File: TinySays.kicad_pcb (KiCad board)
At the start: 2 copper layers, 40 x 40 mm, 31 parts, among them IC1 ATTINY85-S, P1 CONN_02X03, P2 USB_OTG, P3 CONN_01X02, SW1 Switch_SPDT_x2, U1 MCP73831

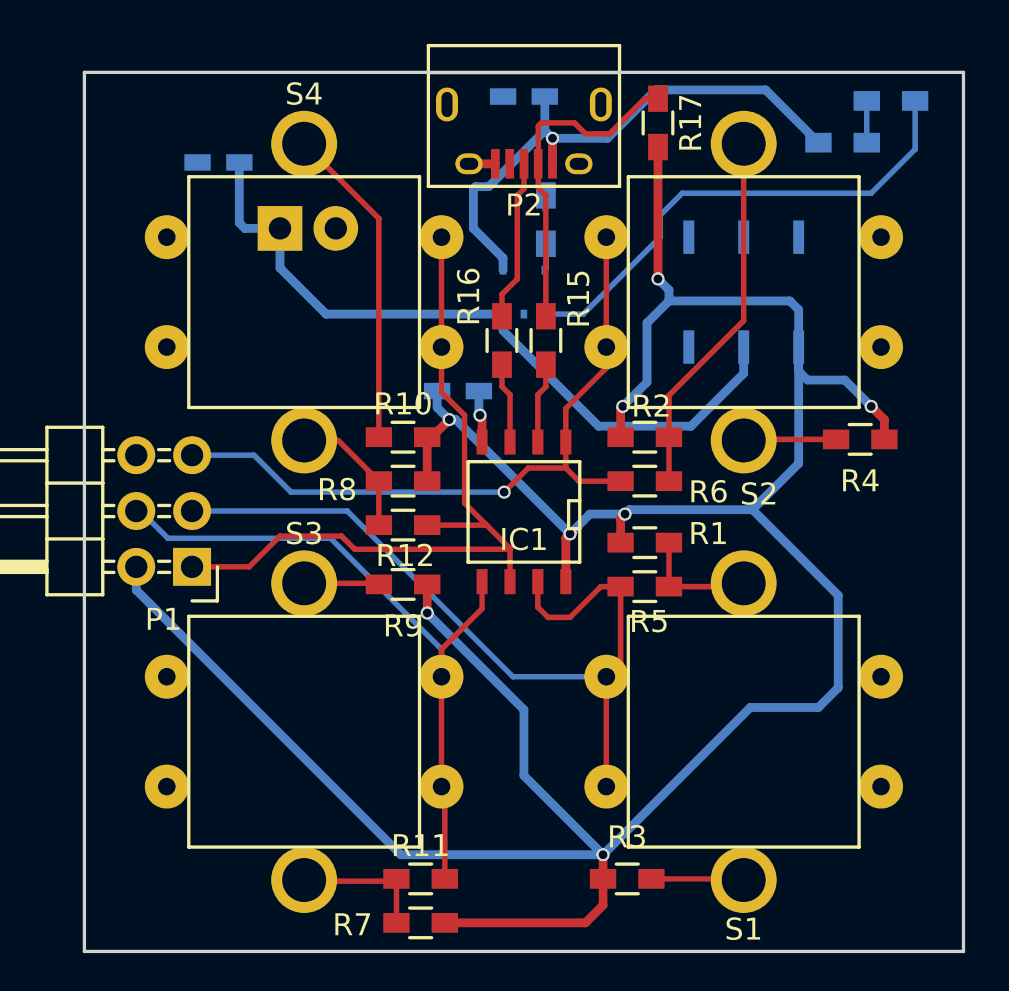
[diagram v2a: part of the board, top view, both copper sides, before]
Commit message: Cleaned up the routing a bit.
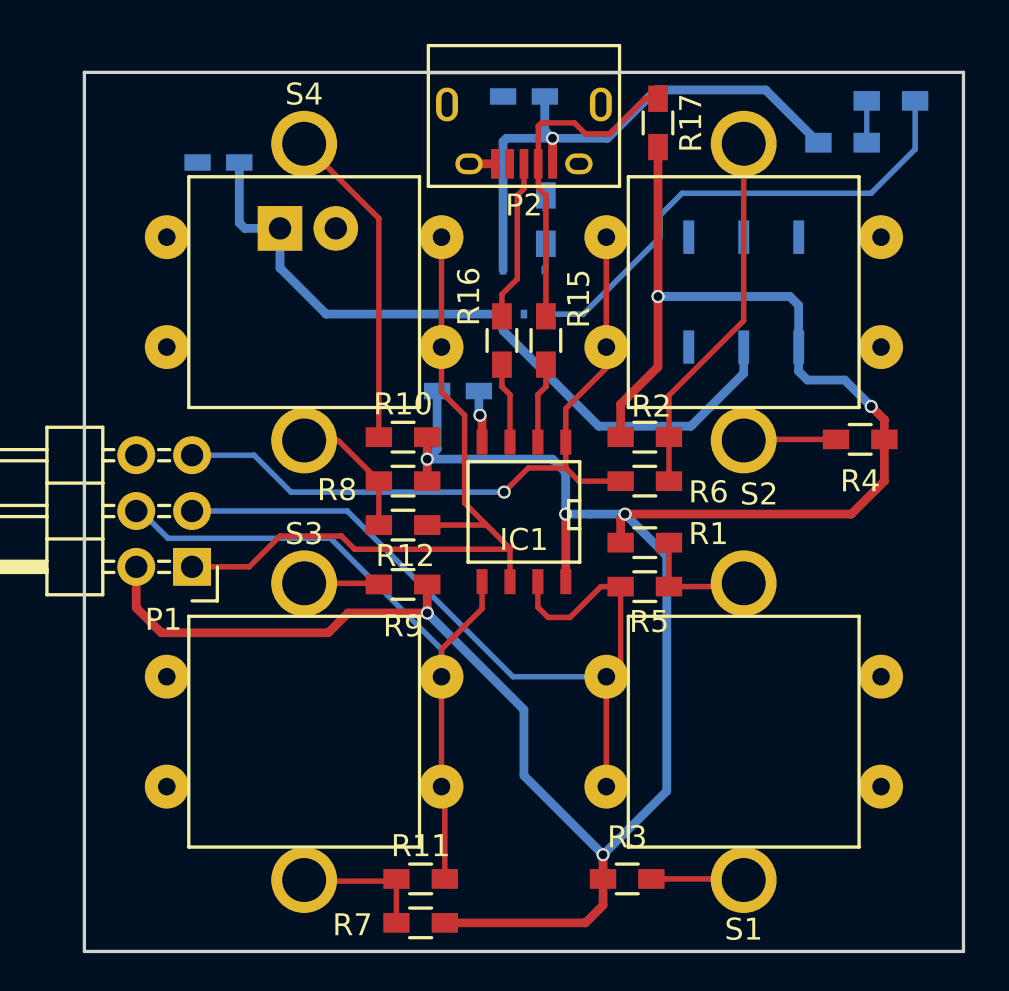
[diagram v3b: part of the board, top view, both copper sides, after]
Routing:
- net VCC: track 138.6 -> 123.8 mm, vias 8 -> 7
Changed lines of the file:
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@@
-(kicad_pcb (version 4) (host pcbnew 4.0.2-stable)
+(kicad_pcb (version 4) (host pcbnew 4.0.2-4+6225~38~ubuntu14.04.1-stable)
   (general
     (links 74)
     (no_connects 0)
-    (area 77.374999 42.175 126.000001 87.075)
+    (area 85.824999 45.424999 125.975001 85.575001)
     (thickness 1.6)
     (drawings 16)
-    (tracks 197)
+    (tracks 190)
     (zones 0)
     (modules 31)
@@
   (gr_line (start 125.9 45.5) (end 125.9 85.5) (angle 90) (layer Edge.Cuts) (width 0.15))
   (gr_line (start 85.9 45.5) (end 125.9 45.5) (angle 90) (layer Edge.Cuts) (width 0.15))
+  (segment (start 104.95 54.5) (end 104.95 48.65) (width 0.4) (layer B.Cu) (net 1))
+  (segment (start 105.1 48.5) (end 107.2 48.5) (width 0.4) (layer B.Cu) (net 1))
+  (segment (start 104.95 48.65) (end 105.1 48.5) (width 0.4) (layer B.Cu) (net 1))
   (segment (start 106.85 46.6) (end 106.85 48.15) (width 0.4) (layer B.Cu) (net 1))
-  (segment (start 106.85 48.15) (end 104.3 50.7) (width 0.4) (layer B.Cu) (net 1))
-  (segment (start 104.95 53.95) (end 104.95 54.5) (width 0.4) (layer B.Cu) (net 1))
-  (segment (start 103.6 52.6) (end 104.95 53.95) (width 0.4) (layer B.Cu) (net 1))
-  (segment (start 103.6 50.8) (end 103.6 52.6) (width 0.4) (layer B.Cu) (net 1))
-  (segment (start 103.7 50.7) (end 103.6 50.8) (width 0.4) (layer B.Cu) (net 1))
-  (segment (start 104.3 50.7) (end 103.7 50.7) (width 0.4) (layer B.Cu) (net 1))
   (segment (start 107.2 48.5) (end 109.7 48.5) (width 0.4) (layer B.Cu) (net 1))
   (segment (start 116.9 46.3) (end 119.3 48.7) (width 0.4) (layer B.Cu) (net 1))
@@
   (segment (start 103.85 61.05) (end 103.9 61.1) (width 0.4) (layer B.Cu) (net 2))
   (segment (start 104.6009 49.66254) (end 103.4009 49.66254) (width 0.4) (layer F.Cu) (net 2))
-  (segment (start 102.5 61.3) (end 102.8 61.3) (width 0.4) (layer B.Cu) (net 3))
-  (segment (start 102.8 61.3) (end 108 66.5) (width 0.4) (layer B.Cu) (net 3))
-  (segment (start 88.26 68) (end 88.26 69.06) (width 0.4) (layer B.Cu) (net 3))
-  (segment (start 100.3 81.1) (end 109.5 81.1) (width 0.4) (layer B.Cu) (net 3))
-  (segment (start 88.26 69.06) (end 100.3 81.1) (width 0.4) (layer B.Cu) (net 3))
+  (segment (start 118.4 58) (end 118.4 56.1) (width 0.4) (layer B.Cu) (net 3) (status 400000))
+  (via (at 112 55.7) (size 0.6) (drill 0.4) (layers F.Cu B.Cu) (net 3))
+  (segment (start 118 55.7) (end 112 55.7) (width 0.4) (layer B.Cu) (net 3))
+  (segment (start 118.4 56.1) (end 118 55.7) (width 0.4) (layer B.Cu) (net 3))
+  (segment (start 112 48.9) (end 112 55.7) (width 0.4) (layer F.Cu) (net 3) (status 400000))
+  (segment (start 112 55.7) (end 112 58.9) (width 0.4) (layer F.Cu) (net 3))
+  (segment (start 112 58.9) (end 110.3 60.6) (width 0.4) (layer F.Cu) (net 3))
+  (segment (start 110.3 60.6) (end 110.3 62.1) (width 0.4) (layer F.Cu) (net 3) (status 800000))
+  (segment (start 109.5 81.1) (end 112.4 78.2) (width 0.4) (layer B.Cu) (net 3))
+  (segment (start 112.4 78.2) (end 112.4 67.5) (width 0.4) (layer B.Cu) (net 3))
+  (segment (start 112.4 67.5) (end 110.5 65.6) (width 0.4) (layer B.Cu) (net 3))
+  (segment (start 110.5 65.6) (end 120.8 65.6) (width 0.4) (layer F.Cu) (net 3))
+  (segment (start 122.3 64.1) (end 122.3 62.2) (width 0.4) (layer F.Cu) (net 3))
+  (segment (start 120.8 65.6) (end 122.3 64.1) (width 0.4) (layer F.Cu) (net 3))
+  (segment (start 101.5 70.1) (end 97.9 70.1) (width 0.4) (layer F.Cu) (net 3))
+  (segment (start 88.26 69.86) (end 88.26 68) (width 0.4) (layer F.Cu) (net 3))
+  (segment (start 89.4 71) (end 88.26 69.86) (width 0.4) (layer F.Cu) (net 3))
+  (segment (start 97 71) (end 89.4 71) (width 0.4) (layer F.Cu) (net 3))
+  (segment (start 97.9 70.1) (end 97 71) (width 0.4) (layer F.Cu) (net 3))
+  (segment (start 107.8 65.6) (end 107.8 63.7) (width 0.4) (layer B.Cu) (net 3))
+  (segment (start 107.2 63.1) (end 101.5 63.1) (width 0.4) (layer B.Cu) (net 3))
+  (segment (start 107.8 63.7) (end 107.2 63.1) (width 0.4) (layer B.Cu) (net 3))
+  (via (at 101.5 63.1) (size 0.6) (drill 0.4) (layers F.Cu B.Cu) (net 3))
+  (segment (start 101.95 60) (end 101.95 62.65) (width 0.4) (layer B.Cu) (net 3))
+  (segment (start 101.95 62.65) (end 101.5 63.1) (width 0.4) (layer B.Cu) (net 3))
+  (segment (start 107.805 68.675) (end 107.805 65.605) (width 0.4) (layer F.Cu) (net 3))
+  (via (at 107.8 65.6) (size 0.6) (drill 0.4) (layers F.Cu B.Cu) (net 3))
+  (segment (start 107.805 65.605) (end 107.8 65.6) (width 0.4) (layer F.Cu) (net 3))
   (segment (start 109.5 81.1) (end 105.9 77.5) (width 0.4) (layer B.Cu) (net 3))
-  (segment (start 119.3 74.4) (end 120.2 73.5) (width 0.4) (layer B.Cu) (net 3))
-  (segment (start 116.2 74.4) (end 119.3 74.4) (width 0.4) (layer B.Cu) (net 3))
-  (segment (start 109.5 81.1) (end 116.2 74.4) (width 0.4) (layer B.Cu) (net 3))
   (segment (start 101.5 64.1) (end 101.8 64.1) (width 0.4) (layer F.Cu) (net 3))
   (segment (start 101.5 62.1) (end 101.7 62.1) (width 0.4) (layer F.Cu) (net 3))
-  (segment (start 101.7 62.1) (end 102.5 61.3) (width 0.4) (layer F.Cu) (net 3))
-  (segment (start 101.95 60.75) (end 101.95 60.1) (width 0.4) (layer B.Cu) (net 3))
-  (segment (start 102.5 61.3) (end 101.95 60.75) (width 0.4) (layer B.Cu) (net 3))
-  (via (at 102.5 61.3) (size 0.6) (drill 0.4) (layers F.Cu B.Cu) (net 3))
-  (segment (start 101.5 62.1) (end 101.5 64.1) (width 0.4) (layer F.Cu) (net 3))
+  (segment (start 101.5 62.1) (end 101.5 63.1) (width 0.4) (layer F.Cu) (net 3))
+  (segment (start 101.5 63.1) (end 101.5 64.1) (width 0.4) (layer F.Cu) (net 3))
   (segment (start 101.5 70.1) (end 101.5 68.8) (width 0.4) (layer F.Cu) (net 3))
   (via (at 101.5 70.1) (size 0.6) (drill 0.4) (layers F.Cu B.Cu) (net 3))
@@
   (segment (start 109.5 83.4) (end 108.7 84.2) (width 0.4) (layer F.Cu) (net 3))
   (segment (start 109.5 82.2) (end 109.5 81.1) (width 0.4) (layer F.Cu) (net 3))
-  (segment (start 120.2 69.3) (end 116.3 65.4) (width 0.4) (layer B.Cu) (net 3))
-  (segment (start 120.2 73.5) (end 120.2 69.3) (width 0.4) (layer B.Cu) (net 3))
-  (segment (start 107.805 68.675) (end 107.805 66.695) (width 0.4) (layer F.Cu) (net 3))
-  (segment (start 107.805 66.695) (end 108 66.5) (width 0.4) (layer F.Cu) (net 3))
-  (via (at 108 66.5) (size 0.6) (drill 0.4) (layers F.Cu B.Cu) (net 3))
   (segment (start 108.9 65.6) (end 110.5 65.6) (width 0.4) (layer B.Cu) (net 3))
-  (segment (start 108 66.5) (end 108.9 65.6) (width 0.4) (layer B.Cu) (net 3))
-  (segment (start 118.4 63.3) (end 118.4 58) (width 0.4) (layer B.Cu) (net 3))
-  (segment (start 116.3 65.4) (end 118.4 63.3) (width 0.4) (layer B.Cu) (net 3))
-  (segment (start 110.7 65.4) (end 116.3 65.4) (width 0.4) (layer B.Cu) (net 3))
-  (segment (start 110.5 65.6) (end 110.7 65.4) (width 0.4) (layer B.Cu) (net 3))
+  (segment (start 107.8 65.6) (end 108.9 65.6) (width 0.4) (layer B.Cu) (net 3))
+  (segment (start 110.5 65.6) (end 110.5 65.6) (width 0.4) (layer B.Cu) (net 3))
   (via (at 110.5 65.6) (size 0.6) (drill 0.4) (layers F.Cu B.Cu) (net 3))
+  (segment (start 110.3 66.9) (end 110.3 65.8) (width 0.4) (layer F.Cu) (net 3))
   (segment (start 110.3 65.8) (end 110.5 65.6) (width 0.4) (layer F.Cu) (net 3))
-  (segment (start 110.3 66.9) (end 110.3 65.8) (width 0.4) (layer F.Cu) (net 3))
-  (segment (start 112 48.9) (end 112 54.9) (width 0.4) (layer F.Cu) (net 3))
-  (segment (start 112.5 55.4) (end 112.5 55.9) (width 0.4) (layer B.Cu) (net 3))
-  (segment (start 112 54.9) (end 112.5 55.4) (width 0.4) (layer B.Cu) (net 3))
-  (via (at 112 54.9) (size 0.6) (drill 0.4) (layers F.Cu B.Cu) (net 3))
-  (segment (start 118.4 58) (end 118.4 56.3) (width 0.4) (layer B.Cu) (net 3))
-  (segment (start 110.3 60.8) (end 110.3 62.1) (width 0.4) (layer F.Cu) (net 3))
-  (segment (start 110.4 60.7) (end 110.3 60.8) (width 0.4) (layer F.Cu) (net 3))
-  (via (at 110.4 60.7) (size 0.6) (drill 0.4) (layers F.Cu B.Cu) (net 3))
-  (segment (start 111.5 59.6) (end 110.4 60.7) (width 0.4) (layer B.Cu) (net 3))
-  (segment (start 111.5 56.9) (end 111.5 59.6) (width 0.4) (layer B.Cu) (net 3))
-  (segment (start 112.5 55.9) (end 111.5 56.9) (width 0.4) (layer B.Cu) (net 3))
-  (segment (start 118 55.9) (end 112.5 55.9) (width 0.4) (layer B.Cu) (net 3))
-  (segment (start 118.4 56.3) (end 118 55.9) (width 0.4) (layer B.Cu) (net 3))
   (segment (start 118.4 58) (end 118.4 59.1) (width 0.4) (layer B.Cu) (net 3))
+  (segment (start 122.3 61.3) (end 121.7 60.7) (width 0.4) (layer F.Cu) (net 3))
+  (via (at 121.7 60.7) (size 0.6) (drill 0.4) (layers F.Cu B.Cu) (net 3))
+  (segment (start 121.7 60.7) (end 120.5 59.5) (width 0.4) (layer B.Cu) (net 3))
+  (segment (start 120.5 59.5) (end 118.8 59.5) (width 0.4) (layer B.Cu) (net 3))
+  (segment (start 118.8 59.5) (end 118.4 59.1) (width 0.4) (layer B.Cu) (net 3))
   (segment (start 122.3 62.2) (end 122.3 61.3) (width 0.4) (layer F.Cu) (net 3))
-  (segment (start 118.8 59.5) (end 118.4 59.1) (width 0.4) (layer B.Cu) (net 3))
-  (segment (start 120.5 59.5) (end 118.8 59.5) (width 0.4) (layer B.Cu) (net 3))
-  (segment (start 121.7 60.7) (end 120.5 59.5) (width 0.4) (layer B.Cu) (net 3))
-  (via (at 121.7 60.7) (size 0.6) (drill 0.4) (layers F.Cu B.Cu) (net 3))
-  (segment (start 122.3 61.3) (end 121.7 60.7) (width 0.4) (layer F.Cu) (net 3))
   (segment (start 105.9 77.5) (end 105.9 74.5) (width 0.4) (layer B.Cu) (net 3))
   (via (at 109.5 81.1) (size 0.6) (drill 0.4) (layers F.Cu B.Cu) (net 3))
